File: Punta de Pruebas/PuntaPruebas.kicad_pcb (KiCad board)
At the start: 2 copper layers, 61 x 38.1 mm, 23 parts, among them P1 CONN_2, P2 CONN_1, P3 CONN_1, SW1 Llave Inversora, U1 40106

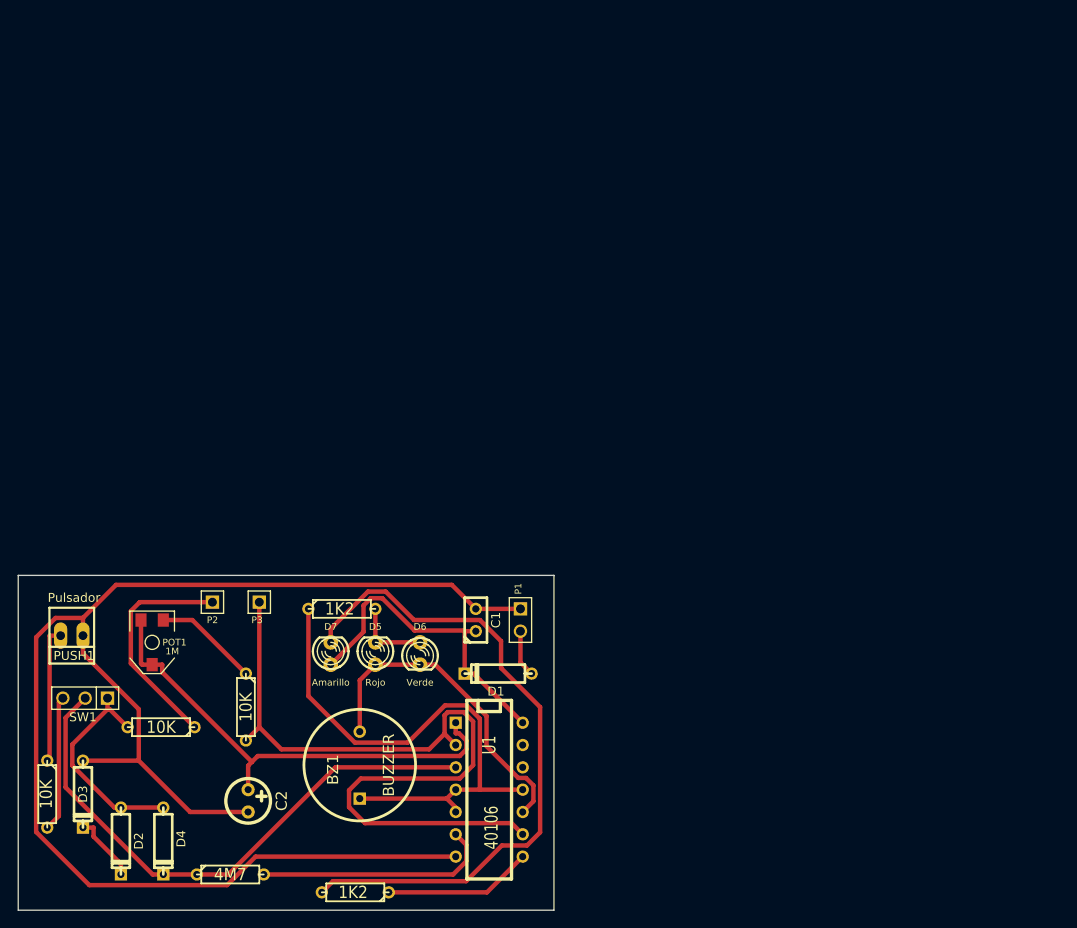
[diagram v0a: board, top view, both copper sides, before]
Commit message: PCB definitivo, incremento ancho de pista y mejoras en los archivos gerber
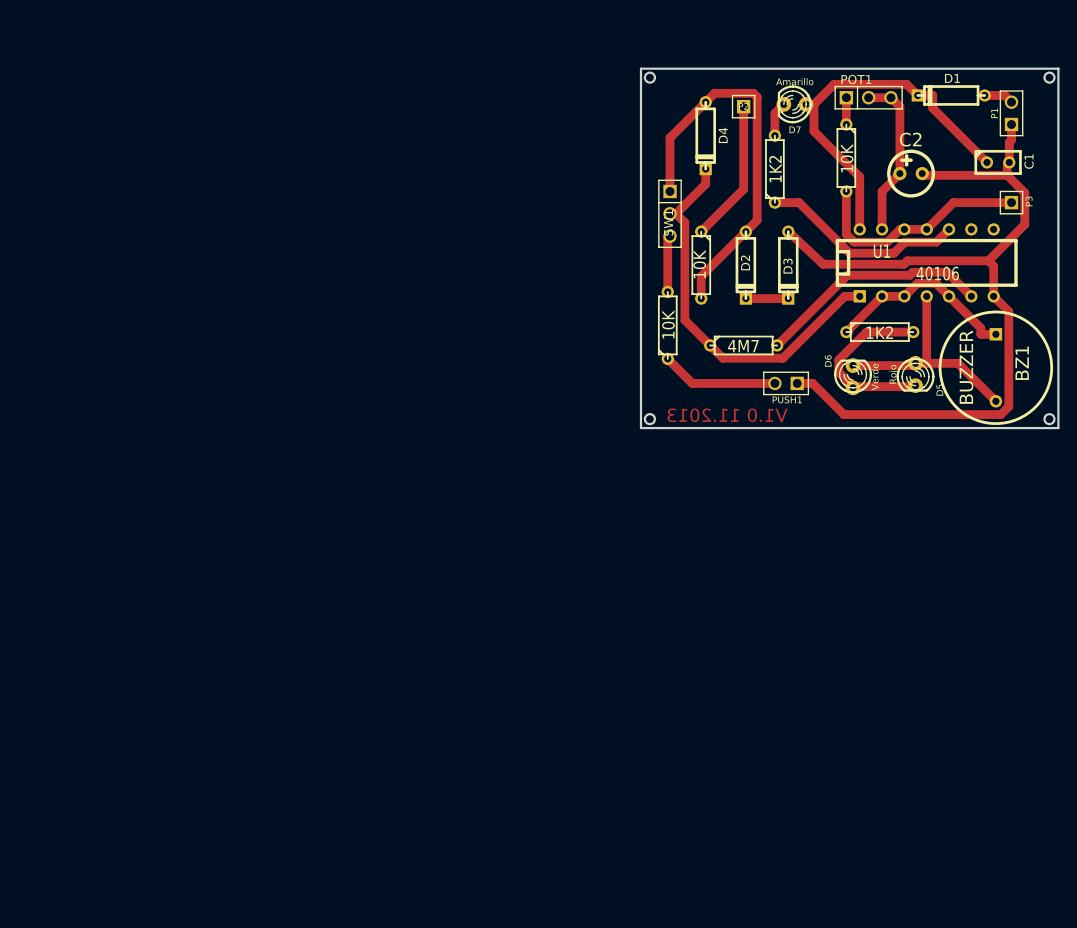
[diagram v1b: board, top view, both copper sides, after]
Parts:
- C2: value CAPAPOL -> 1 uF
- POT1: footprint POT_CMS -> PIN_ARRAY_3X1
- PUSH1: footprint PINHEAD1-2 -> PIN_ARRAY_2X1
- moved C2 103.9 mm to (274.3, 87.6), turned to 0 degrees
- moved POT1 102.4 mm to (269.5, 79.0), turned to 0 degrees
- moved D4 101.3 mm to (251.0, 83.3)
- moved D3 100.3 mm to (260.4, 98.0)
- moved P3 96.9 mm to (285.8, 90.9)
- moved D2 96.7 mm to (255.5, 98.0)
- moved R6 95.1 mm to (258.8, 87.1), turned to 90 degrees
- moved R3 92.6 mm to (267.0, 85.9)
- moved R2 88.5 mm to (246.6, 104.9), turned to 90 degrees
- moved SW1 86.4 mm to (246.9, 92.2), turned to 270 degrees
- moved PUSH1 86.2 mm to (260.1, 111.5)
- moved BZ1 85.3 mm to (284.0, 109.7), turned to 270 degrees
- moved R4 83.9 mm to (255.3, 107.2)
- moved D1 83.6 mm to (278.9, 78.7)
- moved P2 82.7 mm to (255.3, 80.0), turned to 0 degrees
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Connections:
- U1 pad 1: N-0000013 -> N-000008
- U1 pad 10: N-000003 -> N-0000015
- U1 pad 11: N-000002 -> N-0000012
- U1 pad 12: (no net) -> N-0000012
- U1 pad 13: (no net) -> N-0000013
- U1 pad 2: N-0000012 -> N-000002
- U1 pad 3: N-000008 -> N-000002
- U1 pad 4: N-000002 -> N-000003
- U1 pad 8: N-0000015 -> (no net)
- U1 pad 9: N-0000012 -> (no net)
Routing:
- net VSS: track 172.5 -> 95.9 mm
- net N-0000017: track 76.3 -> 3.98 mm
- net N-0000012: track 90.2 -> 25.9 mm
- net N-000002: track 63.0 -> 22.1 mm
- net N-0000013: track 54.8 -> 18.8 mm
- net N-000008: track 64.6 -> 44.3 mm
- net N-000006: track 24.8 -> 43.9 mm
- net N-000001: track 8.89 -> 20.8 mm
- net N-000003: track 37.6 -> 25.8 mm
- net N-0000016: track 25.9 -> 16.2 mm
- net N-0000010: track 15.5 -> 6.46 mm
- net N-0000014: track 11.9 -> 3.05 mm
- net N-0000015: track 16.9 -> 23.3 mm
- net VDD: track 36.8 -> 42.4 mm
- net N-000004: track 7.83 -> 4.83 mm
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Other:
- board size 61 x 38.1 mm -> 47.5 x 40.9 mm
- net class Default: trace_width 0.508 -> 1; via_dia 0.889 -> 1.9; via_drill 0.635 -> 1.2
- rule pad_to_mask_clearance: 0 -> 0.2
- rule trace_min: 0.01 -> 0.254
- rule via_min_size: 0.035 -> 0.889
- board text added: "V1.0 11.2013"

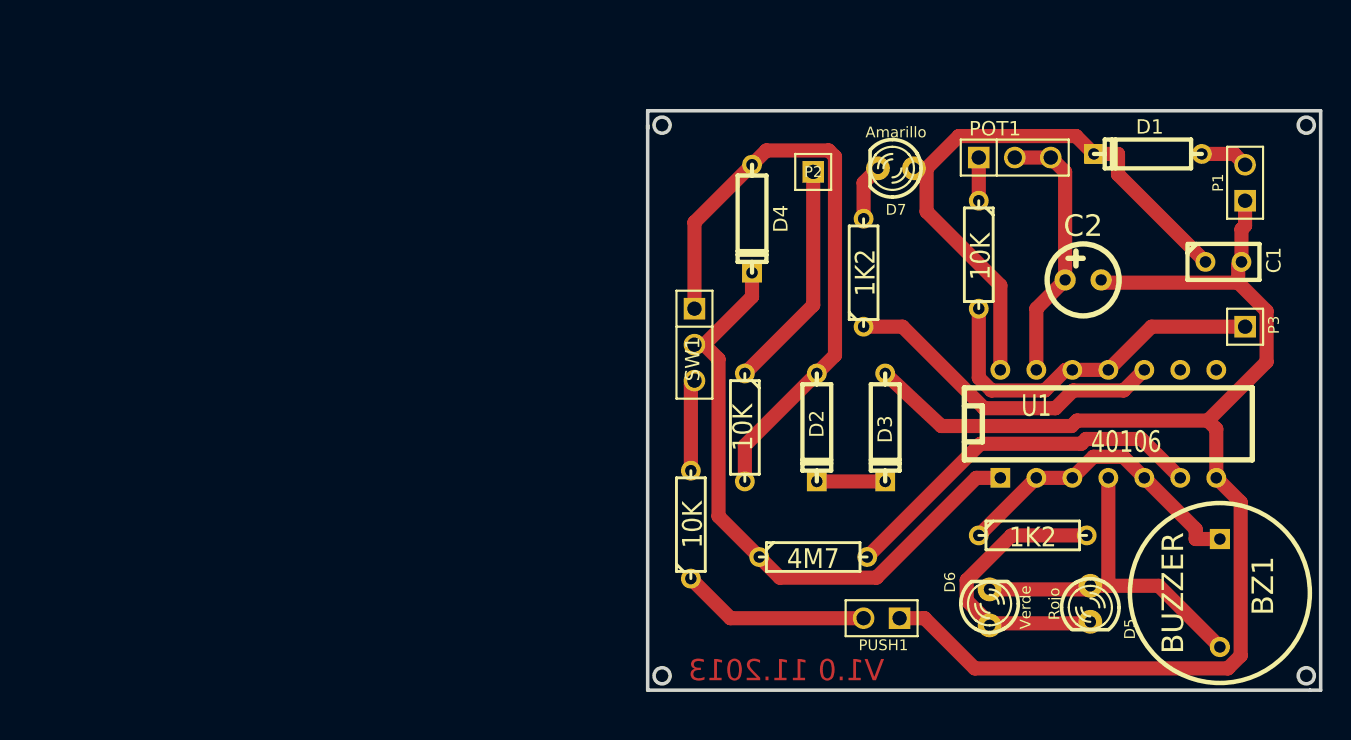
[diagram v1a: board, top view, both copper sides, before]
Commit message: Agrando pistas e impreso para mayor comodidad y adaptarlo al gabinete a usar
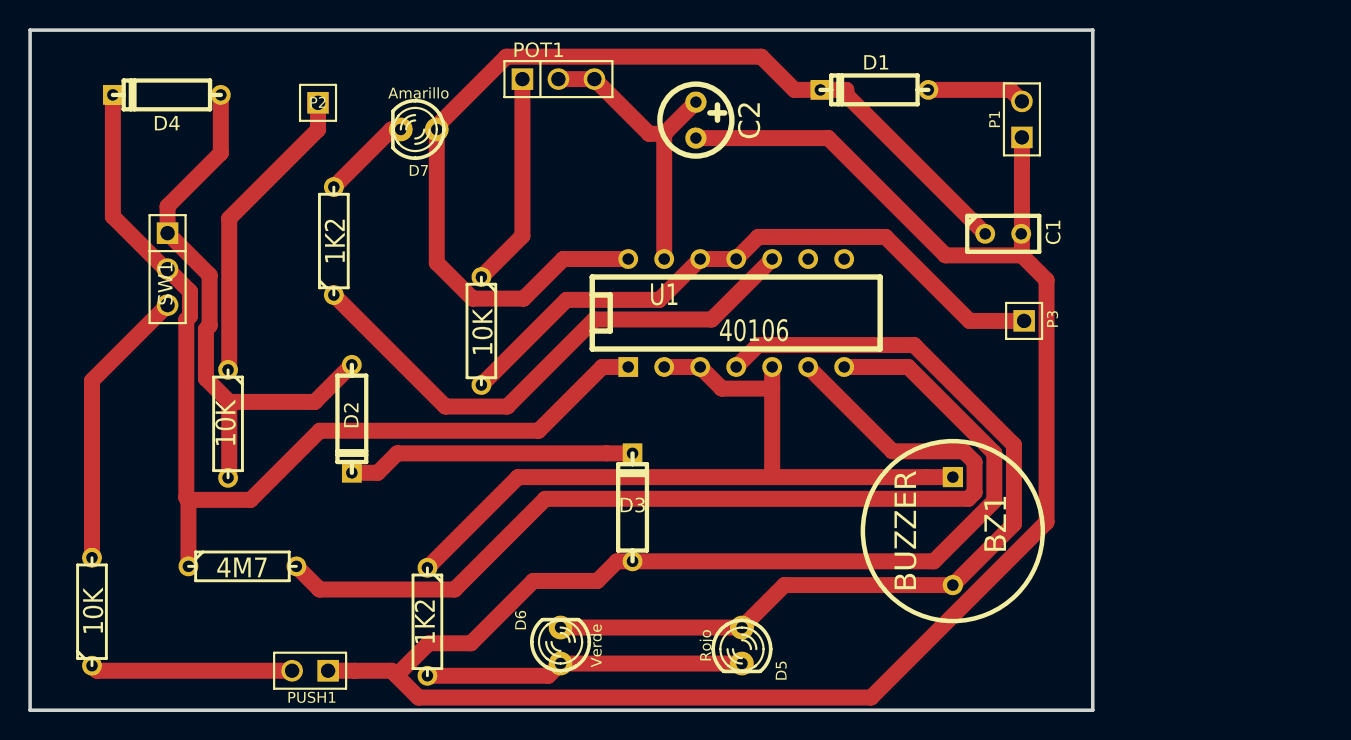
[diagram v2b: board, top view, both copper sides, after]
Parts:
- moved R5 43.2 mm to (228.0, 111.8), turned to 270 degrees
- moved R2 42.7 mm to (204.4, 111.0)
- moved D4 42.2 mm to (209.7, 74.6), turned to 180 degrees
- moved PUSH1 40.5 mm to (219.8, 115.2)
- moved R4 40.3 mm to (215.0, 107.8)
- moved SW1 37.6 mm to (209.7, 86.9)
- moved R6 37.5 mm to (221.4, 84.9)
- moved R1 36.5 mm to (214.0, 97.8)
- moved R3 35.5 mm to (231.9, 91.2)
- moved P2 35.3 mm to (220.3, 75.1)
- moved D7 33.8 mm to (227.4, 77.0)
- moved D2 32.8 mm to (222.7, 97.4)
- moved POT1 32.7 mm to (237.3, 73.5)
- moved D6 30.4 mm to (237.4, 113.4)
- moved C2 29.6 mm to (247.0, 76.4), turned to 270 degrees
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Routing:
- net VSS: track 95.9 -> 174.8 mm
- net N-000009: track 26.7 -> 68.0 mm
- net N-000003: track 25.8 -> 63.8 mm
- net N-000002: track 22.1 -> 55.8 mm
- net VDD: track 42.4 -> 71.5 mm
- net N-000008: track 44.3 -> 70.7 mm
- net N-0000012: track 25.9 -> 45.1 mm
- net N-000004: track 4.83 -> 20.4 mm
- net N-0000015: track 23.3 -> 38.5 mm
- net N-0000010: track 6.46 -> 20.0 mm
- net N-0000014: track 3.05 -> 15.2 mm
- net N-0000016: track 16.2 -> 21.5 mm
- net N-000007: track 3.36 -> 6.94 mm
- net N-000006: track 43.9 -> 40.4 mm
- net N-0000017: track 3.98 -> 6.41 mm
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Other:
- board size 47.5 x 40.9 mm -> 75 x 48 mm
- net class Default: trace_width 1 -> 1.13; via_dia 1.9 -> 2.1; via_drill 1.2 -> 1.7
- board text removed: "V1.0 11.2013"
